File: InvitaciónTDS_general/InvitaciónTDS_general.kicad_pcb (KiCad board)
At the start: 2 copper layers, 95 x 95 mm, 3 parts, among them J1 Conn_01x02_Pin

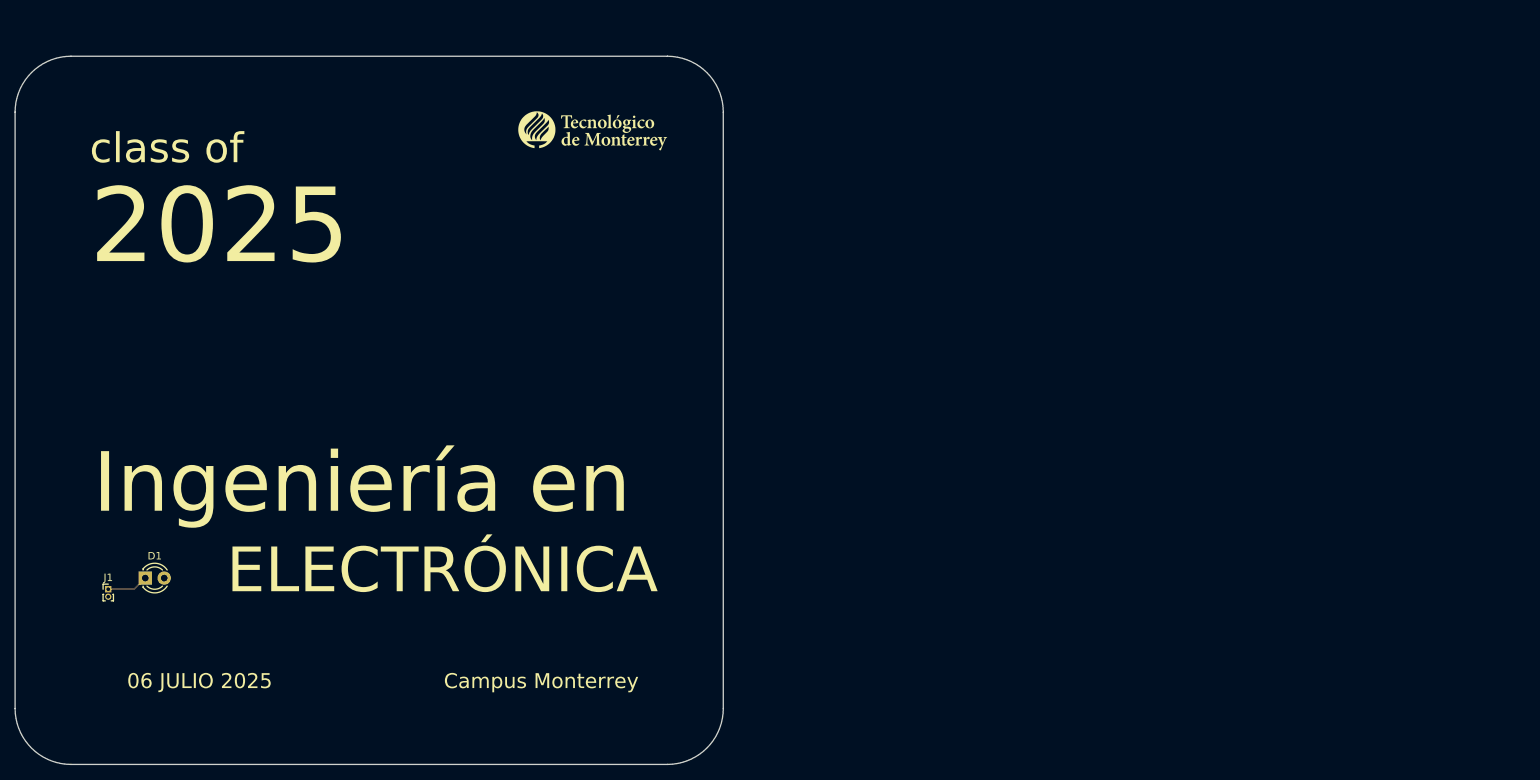
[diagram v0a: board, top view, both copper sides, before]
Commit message: Adición de gráficos frente PCB general
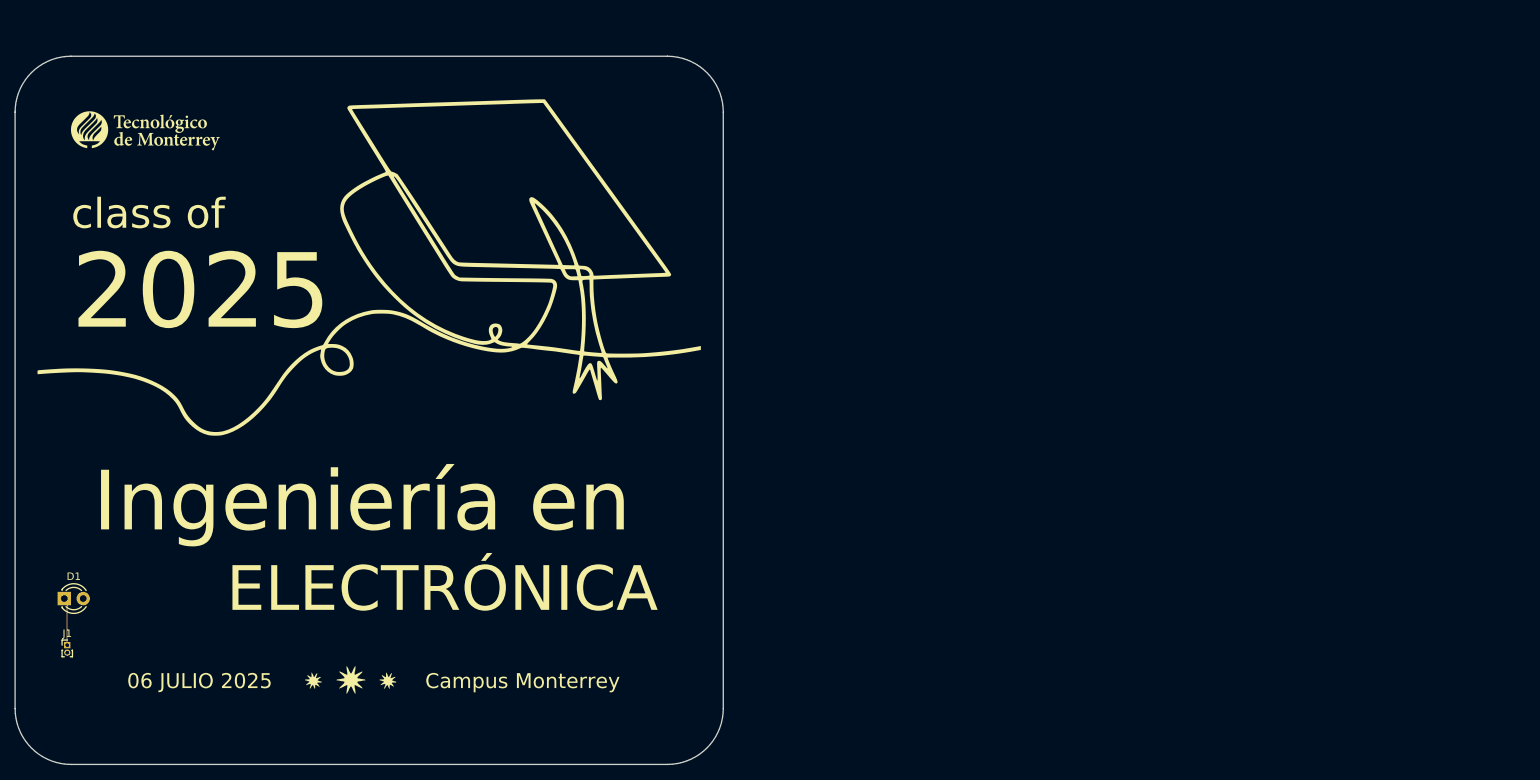
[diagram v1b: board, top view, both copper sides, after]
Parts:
- added G***: LOGO, LOGO, F.Cu at (112.5, 77.5)
- added G***: LOGO, LOGO, F.Cu at (110.0, 135.0)
- moved G*** 60.0 mm to (82.5, 60.0)
- moved D1 11.2 mm to (71.6, 122.8)
- moved J1 9.30 mm to (72.0, 129.0)
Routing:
- net Net-(D1-K): track 5.58 -> 6.42 mm

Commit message: Esquemático actualizado, rev 1, pre-retro
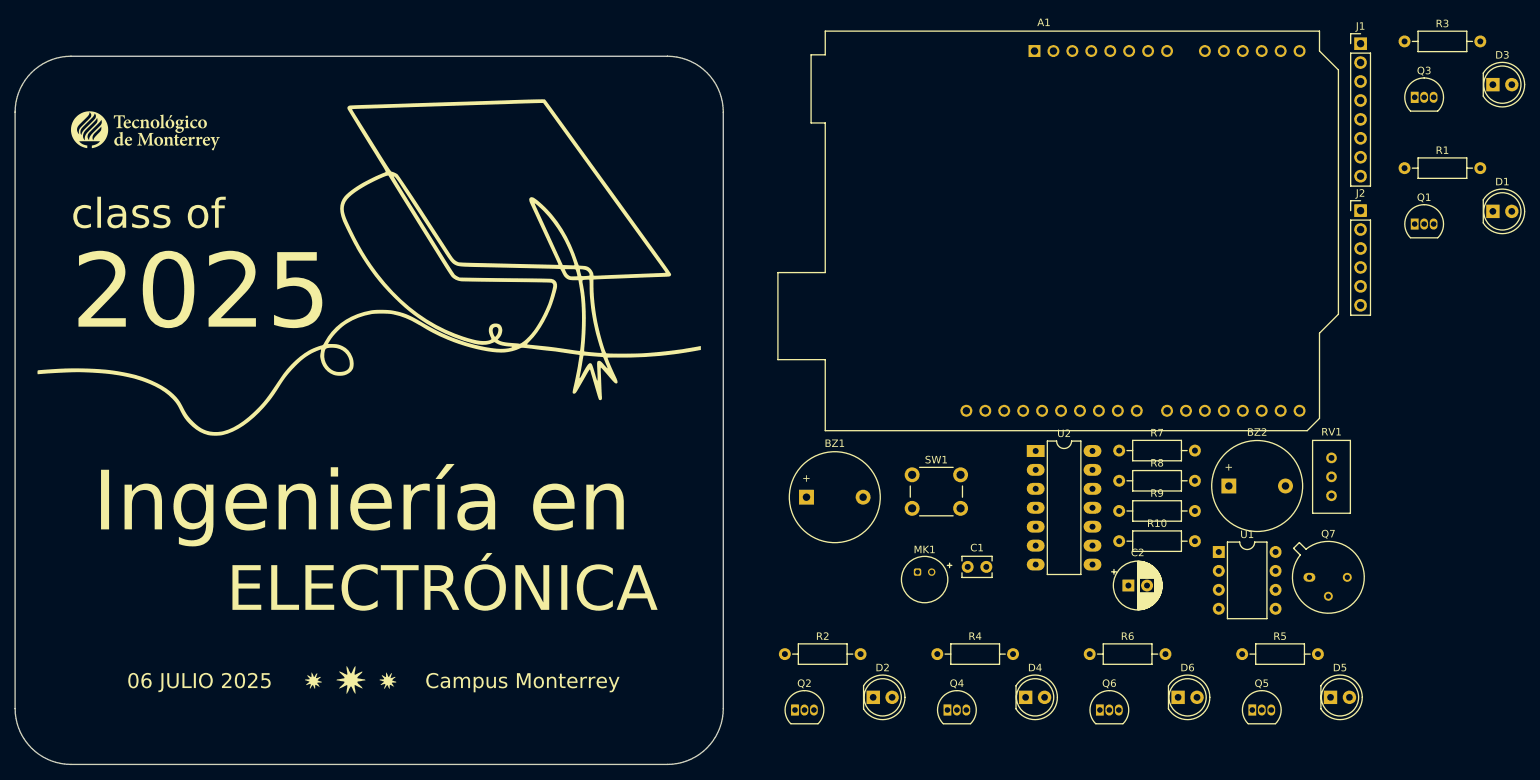
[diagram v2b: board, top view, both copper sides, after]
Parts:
- added A1: Arduino_UNO_R3, Module:Arduino_UNO_R3, F.Cu at (201.8, 49.3)
- added BZ1: Buzzer, Buzzer_Beeper:Buzzer_12x9.5RM7.6, F.Cu at (171.2, 109.2)
- added BZ2: Buzzer, Buzzer_Beeper:Buzzer_12x9.5RM7.6, F.Cu at (227.8, 107.7)
- added C1: C_ceramico, Capacitor_THT:C_Disc_D3.8mm_W2.6mm_P2.50mm, F.Cu at (192.8, 118.5)
- added C2: C_Polarized, Capacitor_THT:CP_Radial_D6.3mm_P2.50mm, F.Cu at (214.3, 121.0)
- added D2: LED, LED_THT:LED_D5.0mm, F.Cu at (180.1, 136.0)
- added D3: LED, LED_THT:LED_D5.0mm, F.Cu at (263.2, 53.8)
- added D4: LED, LED_THT:LED_D5.0mm, F.Cu at (200.6, 136.0)
- added D5: LED, LED_THT:LED_D5.0mm, F.Cu at (241.5, 136.0)
- added D6: LED, LED_THT:LED_D5.0mm, F.Cu at (221.0, 136.0)
- added J2: FTDI Connector, Connector_PinHeader_2.54mm:PinHeader_1x06_P2.54mm_Vertical, F.Cu at (245.5, 70.7)
- added MK1: Microphone, Sensor_Audio:POM-2244P-C3310-2-R, F.Cu at (186.1, 119.2)
- added Q1: 2N2219, Package_TO_SOT_THT:TO-92_Inline, F.Cu at (252.8, 72.5)
- added Q2: 2N2219, Package_TO_SOT_THT:TO-92_Inline, F.Cu at (169.6, 137.7)
- added Q3: 2N2219, Package_TO_SOT_THT:TO-92_Inline, F.Cu at (252.8, 55.5)
- added Q4: 2N2219, Package_TO_SOT_THT:TO-92_Inline, F.Cu at (190.1, 137.7)
- added Q5: 2N2219, Package_TO_SOT_THT:TO-92_Inline, F.Cu at (231.0, 137.7)
- added Q6: 2N2219, Package_TO_SOT_THT:TO-92_Inline, F.Cu at (210.5, 137.7)
- added Q7: 2N2219, Package_TO_SOT_THT:TO-39-3, F.Cu at (238.6, 119.9)
- added R1: R, Resistor_THT:R_Axial_DIN0207_L6.3mm_D2.5mm_P10.16mm_Horizontal, F.Cu at (251.4, 65.0)
- added R10: R, Resistor_THT:R_Axial_DIN0207_L6.3mm_D2.5mm_P10.16mm_Horizontal, F.Cu at (213.1, 115.0)
- added R2: R, Resistor_THT:R_Axial_DIN0207_L6.3mm_D2.5mm_P10.16mm_Horizontal, F.Cu at (168.3, 130.2)
- added R3: R, Resistor_THT:R_Axial_DIN0207_L6.3mm_D2.5mm_P10.16mm_Horizontal, F.Cu at (251.4, 48.0)
- added R4: R, Resistor_THT:R_Axial_DIN0207_L6.3mm_D2.5mm_P10.16mm_Horizontal, F.Cu at (188.7, 130.2)
- added R5: R, Resistor_THT:R_Axial_DIN0207_L6.3mm_D2.5mm_P10.16mm_Horizontal, F.Cu at (229.6, 130.2)
- added R6: R, Resistor_THT:R_Axial_DIN0207_L6.3mm_D2.5mm_P10.16mm_Horizontal, F.Cu at (209.2, 130.2)
- added R7: R, Resistor_THT:R_Axial_DIN0207_L6.3mm_D2.5mm_P10.16mm_Horizontal, F.Cu at (213.1, 102.9)
- added R8: R, Resistor_THT:R_Axial_DIN0207_L6.3mm_D2.5mm_P10.16mm_Horizontal, F.Cu at (213.1, 107.0)
- added R9: R, Resistor_THT:R_Axial_DIN0207_L6.3mm_D2.5mm_P10.16mm_Horizontal, F.Cu at (213.1, 111.0)
- added RV1: R_Potentiometer, Potentiometer_THT:Potentiometer_Bourns_3386C_Horizontal, F.Cu at (241.6, 103.9)
- added SW1: SW_Push, Button_Switch_THT:SW_PUSH_6mm, F.Cu at (185.3, 106.2)
- added U1: LM358, Package_DIP:DIP-8_W7.62mm, F.Cu at (226.5, 116.5)
- added U2: 74LS08, Package_DIP:DIP-14_W7.62mm_LongPads, F.Cu at (201.9, 103.0)
- D1: footprint LED_THT:LED_D3.0mm -> LED_THT:LED_D5.0mm
- J1: value Conn_01x02_Pin -> Voltage Conn; footprint Connector_PinHeader_1.00mm:PinHeader_1x02_P1.00mm_Vertical -> Connector_PinHeader_2.54mm:PinHeader_1x08_P2.54mm_Vertical
- moved D1 198.6 mm to (263.2, 70.8)
- moved J1 191.3 mm to (245.5, 48.3)
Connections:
- D1 pad 2: unconnected-(D1-A-Pad2) -> /LEDSchem/PinName
- J1 pad 1: Net-(D1-K) -> /LEDSchem/PinName
- J1 pad 2: unconnected-(J1-Pin_2-Pad2) -> GND
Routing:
- net Net-(D1-K): track 6.42 -> 0.00 mm
